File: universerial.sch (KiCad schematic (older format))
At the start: 11 parts

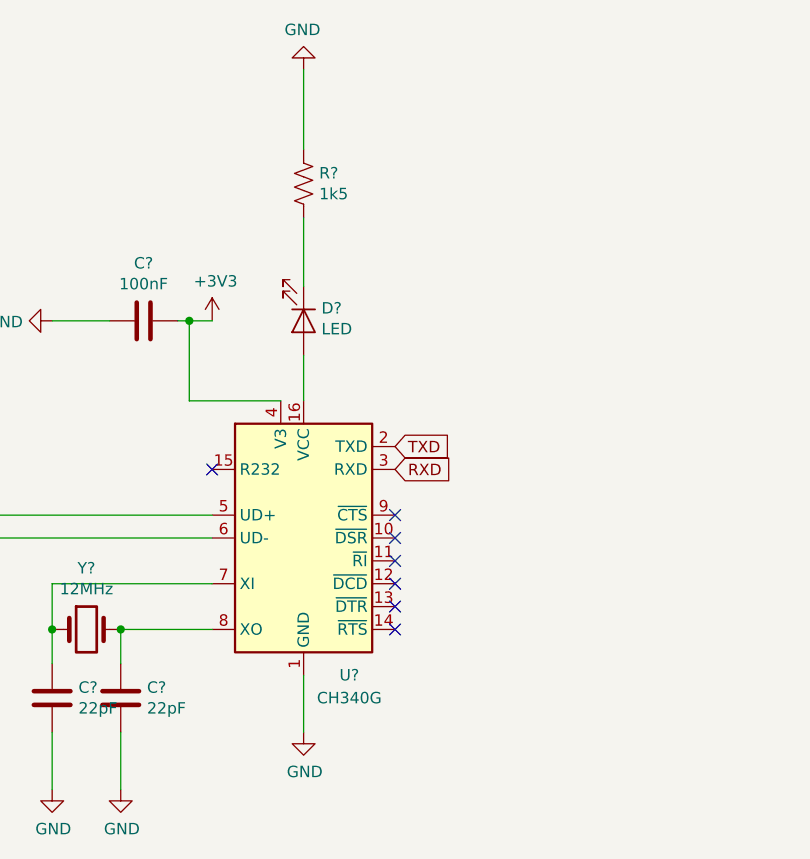
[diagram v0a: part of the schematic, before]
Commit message: Fix VCC placement.
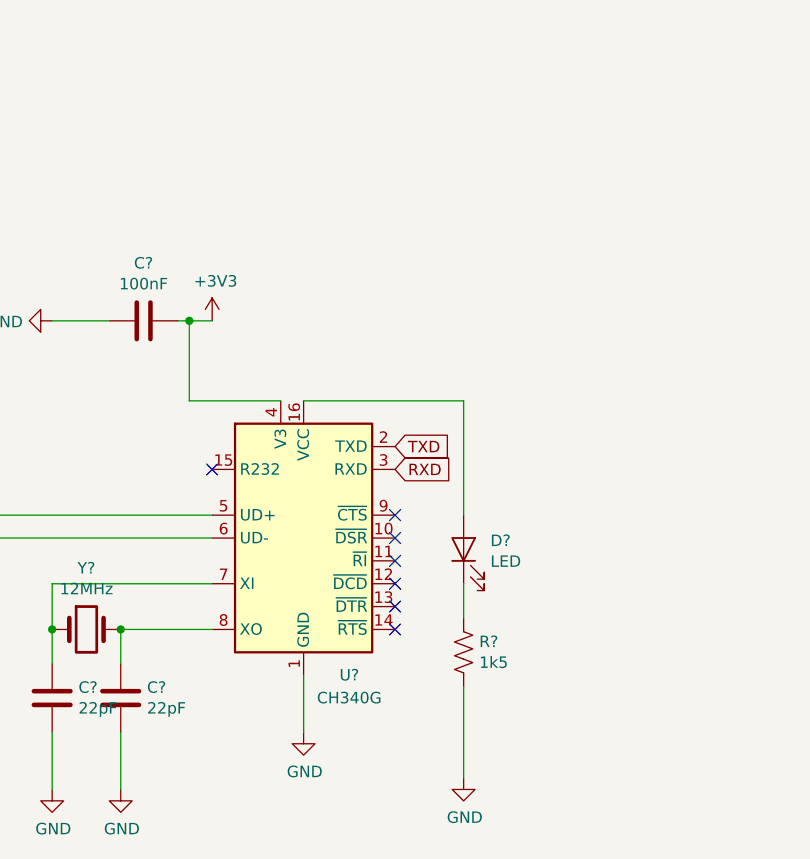
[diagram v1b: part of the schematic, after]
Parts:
- removed D?: LED, symbol Device:LED
- removed R?: 1k5, symbol Device:R_US
- added D?: LED, symbol Device:LED
- added R?: 1k5, symbol Device:R_US
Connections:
- net GND: now also R?.1
- net at U?.16 (VCC): now also D?.2 (A)
- new net: D?.1 (K), R?.2
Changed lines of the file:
@@
 	4950 2900 4900 2900
-$Comp
-L Device:LED D?
-U 1 1 610C1465
-P 5450 2900
-F 0 "D?" V 5395 2978 50  0000 L CNN
-F 1 "LED" V 5486 2978 50  0000 L CNN
-F 2 "" H 5450 2900 50  0001 C CNN
-F 3 "~" H 5450 2900 50  0001 C CNN
-	1    5450 2900
-	0    1    1    0
-$EndComp
-$Comp
-L Device:R_US R?
-U 1 1 610C1517
-P 5450 2300
-F 0 "R?" H 5518 2346 50  0000 L CNN
-F 1 "1k5" H 5518 2255 50  0000 L CNN
-F 2 "" V 5490 2290 50  0001 C CNN
-F 3 "~" H 5450 2300 50  0001 C CNN
-	1    5450 2300
-	1    0    0    -1
-$EndComp
-$Comp
-L power:GND #PWR?
-U 1 1 610C1658
-P 5450 1800
-F 0 "#PWR?" H 5450 1550 50  0001 C CNN
-F 1 "GND" H 5455 1627 50  0000 C CNN
-F 2 "" H 5450 1800 50  0001 C CNN
-F 3 "" H 5450 1800 50  0001 C CNN
-	1    5450 1800
-	-1   0    0    1
-$EndComp
-Wire Wire Line
-	5450 3250 5450 3050
-Wire Wire Line
-	5450 2750 5450 2450
-Wire Wire Line
-	5450 2150 5450 1800
 $Comp
 L Device:Crystal Y?
@@
 NoConn ~ 5850 3950
 NoConn ~ 5850 4050
+$Comp
+L Device:LED D?
+U 1 1 610C66BC
+P 6150 3900
+F 0 "D?" V 6188 3783 50  0000 R CNN
+F 1 "LED" V 6097 3783 50  0000 R CNN
+F 2 "" H 6150 3900 50  0001 C CNN
+F 3 "~" H 6150 3900 50  0001 C CNN
+	1    6150 3900
+	0    -1   -1   0
+$EndComp
+$Comp
+L Device:R_US R?
+U 1 1 610C671C
+P 6150 4350
+F 0 "R?" H 6082 4304 50  0000 R CNN
+F 1 "1k5" H 6082 4395 50  0000 R CNN
+F 2 "" V 6190 4340 50  0001 C CNN
+F 3 "~" H 6150 4350 50  0001 C CNN
+	1    6150 4350
+	-1   0    0    1
+$EndComp
+$Comp
+L power:GND #PWR?
+U 1 1 610C67B6
+P 6150 4900
+F 0 "#PWR?" H 6150 4650 50  0001 C CNN
+F 1 "GND" H 6155 4727 50  0000 C CNN
+F 2 "" H 6150 4900 50  0001 C CNN
+F 3 "" H 6150 4900 50  0001 C CNN
+	1    6150 4900
+	1    0    0    -1
+$EndComp
+Wire Wire Line
+	5450 3250 6150 3250
+Wire Wire Line
+	6150 3250 6150 3750
+Wire Wire Line
+	6150 4050 6150 4200
+Wire Wire Line
+	6150 4500 6150 4900
 $EndSCHEMATC

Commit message: Finish schematic.
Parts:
- added C?: 100nF, symbol Device:C
- added D? (x2): D, symbol Device:D
- added D? (x2): LED, symbol Device:LED
- added R? (x3): 1k5, symbol Device:R_US
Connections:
- net RXD is gone; now on an unnamed net: U?.3 (RXD)
- net +3V3: now also J?.3 (Pin_3)
- net +5V: now also J?.1 (Pin_1), D?.2 (A)
- net GND: now also J?.6 (Pin_6), C?.2
- net at D?.2 (A), U?.16 (VCC): now also J?.2 (Pin_2), C?.1, D?.1 (K), R?.1, R?.1
- net at J?.4 (Pin_4): now also R?.1
- net at J?.5 (Pin_5): now also D?.1 (K)
- net TXD: no longer names the net of U?.2 (TXD)
- net TXD: now also D?.1 (K), R?.2
- new net: D?.1 (K), D?.2 (A)
- new net: D?.2 (A), R?.2 (x2)
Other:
- moved on the sheet: C?, D?, J?, R?

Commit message: Annotate schematic.
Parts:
- gave numbers to parts that had none: 19
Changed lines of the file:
@@
 NoConn ~ 9500 3500
 $Comp
-L Connector_Generic:Conn_01x06 J?
+L Connector_Generic:Conn_01x06 J2
 U 1 1 610BFF68
 P 7800 3350
-F 0 "J?" H 7880 3342 50  0000 L CNN
+F 0 "J2" H 7880 3342 50  0000 L CNN
 F 1 "Conn_01x06" H 7880 3251 50  0000 L CNN
 F 2 "" H 7800 3350 50  0001 C CNN
@@
 $EndComp
 $Comp
-L Connector:USB_A J?
+L Connector:USB_A J1
 U 1 1 610C021E
 P 2800 3750
-F 0 "J?" H 2855 4217 50  0000 C CNN
+F 0 "J1" H 2855 4217 50  0000 C CNN
 F 1 "USB_A" H 2855 4126 50  0000 C CNN
 F 2 "" H 2950 3700 50  0001 C CNN
@@
 $EndComp
 $Comp
-L power:+5V #PWR?
+L power:+5V #PWR03
 U 1 1 610C0316
 P 3700 3150
-F 0 "#PWR?" H 3700 3000 50  0001 C CNN
+F 0 "#PWR03" H 3700 3000 50  0001 C CNN
 F 1 "+5V" H 3715 3323 50  0000 C CNN
 F 2 "" H 3700 3150 50  0001 C CNN
@@
 	3100 3550 3300 3550
 $Comp
-L power:GND #PWR?
+L power:GND #PWR01
 U 1 1 610C03FA
 P 2800 4350
-F 0 "#PWR?" H 2800 4100 50  0001 C CNN
+F 0 "#PWR01" H 2800 4100 50  0001 C CNN
 F 1 "GND" H 2805 4177 50  0000 C CNN
 F 2 "" H 2800 4350 50  0001 C CNN
@@
 	2800 4250 2800 4350
 $Comp
-L Device:C C?
+L Device:C C1
 U 1 1 610C04CB
 P 3300 4400
-F 0 "C?" H 3415 4446 50  0000 L CNN
+F 0 "C1" H 3415 4446 50  0000 L CNN
 F 1 "10uF" H 3415 4355 50  0000 L CNN
 F 2 "" H 3338 4250 50  0001 C CNN
@@
 	3300 3550 3300 4250
 $Comp
-L power:GND #PWR?
+L power:GND #PWR02
 U 1 1 610C055C
 P 3300 4800
-F 0 "#PWR?" H 3300 4550 50  0001 C CNN
+F 0 "#PWR02" H 3300 4550 50  0001 C CNN
 F 1 "GND" H 3305 4627 50  0000 C CNN
 F 2 "" H 3300 4800 50  0001 C CNN
@@
 	3300 4550 3300 4800
 $Comp
-L Device:C C?
+L Device:C C2
 U 1 1 610C09D3
 P 3700 4400
-F 0 "C?" H 3815 4446 50  0000 L CNN
+F 0 "C2" H 3815 4446 50  0000 L CNN
 F 1 "100nF" H 3815 4355 50  0000 L CNN
 F 2 "" H 3738 4250 50  0001 C CNN
@@
 $EndComp
 $Comp
-L power:GND #PWR?
+L power:GND #PWR04
 U 1 1 610C0A9A
 P 3700 4800
-F 0 "#PWR?" H 3700 4550 50  0001 C CNN
+F 0 "#PWR04" H 3700 4550 50  0001 C CNN
 F 1 "GND" H 3705 4627 50  0000 C CNN
 F 2 "" H 3700 4800 50  0001 C CNN
@@
 	3700 3550 3700 4250
 $Comp
-L power:+3V3 #PWR?
+L power:+3V3 #PWR08
 U 1 1 610C0EF4
 P 5050 2900
-F 0 "#PWR?" H 5050 2750 50  0001 C CNN
+F 0 "#PWR08" H 5050 2750 50  0001 C CNN
 F 1 "+3V3" H 5065 3073 50  0000 C CNN
 F 2 "" H 5050 2900 50  0001 C CNN
@@
 $EndComp
 $Comp
-L Device:C C?
+L Device:C C5
 U 1 1 610C0F5D
 P 4750 2900
-F 0 "C?" V 4498 2900 50  0000 C CNN
+F 0 "C5" V 4498 2900 50  0000 C CNN
 F 1 "100nF" V 4589 2900 50  0000 C CNN
 F 2 "" H 4788 2750 50  0001 C CNN
@@
 $EndComp
 $Comp
-L power:GND #PWR?
+L power:GND #PWR05
 U 1 1 610C0FF6
 P 4350 2900
-F 0 "#PWR?" H 4350 2650 50  0001 C CNN
+F 0 "#PWR05" H 4350 2650 50  0001 C CNN
 F 1 "GND" V 4355 2772 50  0000 R CNN
 F 2 "" H 4350 2900 50  0001 C CNN
@@
 	4950 2900 4900 2900
 $Comp
-L Device:Crystal Y?
+L Device:Crystal Y1
 U 1 1 610C1DB2
 P 4500 4250
-F 0 "Y?" H 4500 4518 50  0000 C CNN
+F 0 "Y1" H 4500 4518 50  0000 C CNN
 F 1 "12MHz" H 4500 4427 50  0000 C CNN
 F 2 "" H 4500 4250 50  0001 C CNN
@@
 $EndComp
 $Comp
-L power:GND #PWR?
+L power:GND #PWR09
 U 1 1 610C3384
 P 5450 4700
-F 0 "#PWR?" H 5450 4450 50  0001 C CNN
+F 0 "#PWR09" H 5450 4450 50  0001 C CNN
 F 1 "GND" H 5455 4527 50  0000 C CNN
 F 2 "" H 5450 4700 50  0001 C CNN
@@
 	5050 4250 4650 4250
 $Comp
-L Device:C C?
+L Device:C C3
 U 1 1 610C3F04
 P 4350 4550
-F 0 "C?" H 4465 4596 50  0000 L CNN
+F 0 "C3" H 4465 4596 50  0000 L CNN
 F 1 "22pF" H 4465 4505 50  0000 L CNN
 F 2 "" H 4388 4400 50  0001 C CNN
@@
 $EndComp
 $Comp
-L Device:C C?
+L Device:C C4
 U 1 1 610C3F3C
 P 4650 4550
-F 0 "C?" H 4765 4596 50  0000 L CNN
+F 0 "C4" H 4765 4596 50  0000 L CNN
 F 1 "22pF" H 4765 4505 50  0000 L CNN
 F 2 "" H 4688 4400 50  0001 C CNN
@@
 $EndComp
 $Comp
-L power:GND #PWR?
+L power:GND #PWR06
 U 1 1 610C3FDC
 P 4350 4950
-F 0 "#PWR?" H 4350 4700 50  0001 C CNN
+F 0 "#PWR06" H 4350 4700 50  0001 C CNN
 F 1 "GND" H 4355 4777 50  0000 C CNN
 F 2 "" H 4350 4950 50  0001 C CNN
@@
 $EndComp
 $Comp
-L power:GND #PWR?
+L power:GND #PWR07
 U 1 1 610C4004
 P 4650 4950
-F 0 "#PWR?" H 4650 4700 50  0001 C CNN
+F 0 "#PWR07" H 4650 4700 50  0001 C CNN
 F 1 "GND" H 4655 4777 50  0000 C CNN
 F 2 "" H 4650 4950 50  0001 C CNN
@@
 NoConn ~ 5850 4050
 $Comp
-L Device:LED D?
+L Device:LED D1
 U 1 1 610C66BC
 P 6000 3900
-F 0 "D?" V 6038 3783 50  0000 R CNN
+F 0 "D1" V 6038 3783 50  0000 R CNN
 F 1 "LED" V 5947 3783 50  0000 R CNN
 F 2 "" H 6000 3900 50  0001 C CNN
@@
 $EndComp
 $Comp
-L Device:R_US R?
+L Device:R_US R1
 U 1 1 610C671C
 P 6000 4350
-F 0 "R?" H 5932 4304 50  0000 R CNN
+F 0 "R1" H 5932 4304 50  0000 R CNN
 F 1 "1k5" H 5932 4395 50  0000 R CNN
 F 2 "" V 6040 4340 50  0001 C CNN
@@
 $EndComp
 $Comp
-L power:GND #PWR?
+L power:GND #PWR010
 U 1 1 610C67B6
 P 6000 4900
-F 0 "#PWR?" H 6000 4650 50  0001 C CNN
+F 0 "#PWR010" H 6000 4650 50  0001 C CNN
 F 1 "GND" H 6005 4727 50  0000 C CNN
 F 2 "" H 6000 4900 50  0001 C CNN
@@
 	6000 4500 6000 4900
 $Comp
-L power:+5V #PWR?
+L power:+5V #PWR014
 U 1 1 610C98EA
 P 7600 2850
-F 0 "#PWR?" H 7600 2700 50  0001 C CNN
+F 0 "#PWR014" H 7600 2700 50  0001 C CNN
 F 1 "+5V" H 7615 3023 50  0000 C CNN
 F 2 "" H 7600 2850 50  0001 C CNN
@@
 	7600 3150 7600 2850
 $Comp
-L power:GND #PWR?
+L power:GND #PWR015
 U 1 1 610C9D6A
 P 7600 3950
-F 0 "#PWR?" H 7600 3700 50  0001 C CNN
+F 0 "#PWR015" H 7600 3700 50  0001 C CNN
 F 1 "GND" H 7605 3777 50  0000 C CNN
 F 2 "" H 7600 3950 50  0001 C CNN
@@
 	7600 3650 7600 3950
 $Comp
-L power:+3V3 #PWR?
+L power:+3V3 #PWR013
 U 1 1 610CA266
 P 7450 3350
-F 0 "#PWR?" H 7450 3200 50  0001 C CNN
+F 0 "#PWR013" H 7450 3200 50  0001 C CNN
 F 1 "+3V3" H 7465 3523 50  0000 C CNN
 F 2 "" H 7450 3350 50  0001 C CNN
@@
 	7450 3350 7600 3350
 $Comp
-L Device:R_US R?
+L Device:R_US R4
 U 1 1 610CA74E
 P 7200 3450
-F 0 "R?" V 6995 3450 50  0000 C CNN
+F 0 "R4" V 6995 3450 50  0000 C CNN
 F 1 "1k5" V 7086 3450 50  0000 C CNN
 F 2 "" V 7240 3440 50  0001 C CNN
@@
 	5850 3450 6500 3450
 $Comp
-L Device:D D?
+L Device:D D5
 U 1 1 610CD045
 P 7050 2400
-F 0 "D?" H 7050 2184 50  0000 C CNN
+F 0 "D5" H 7050 2184 50  0000 C CNN
 F 1 "D" H 7050 2275 50  0000 C CNN
 F 2 "" H 7050 2400 50  0001 C CNN
@@
 $EndComp
 $Comp
-L Device:D D?
+L Device:D D3
 U 1 1 610CD0CD
 P 6600 2400
-F 0 "D?" H 6600 2184 50  0000 C CNN
+F 0 "D3" H 6600 2184 50  0000 C CNN
 F 1 "D" H 6600 2275 50  0000 C CNN
 F 2 "" H 6600 2400 50  0001 C CNN
@@
 $EndComp
 $Comp
-L power:+5V #PWR?
+L power:+5V #PWR012
 U 1 1 610CD241
 P 6300 2400
-F 0 "#PWR?" H 6300 2250 50  0001 C CNN
+F 0 "#PWR012" H 6300 2250 50  0001 C CNN
 F 1 "+5V" H 6315 2573 50  0000 C CNN
 F 2 "" H 6300 2400 50  0001 C CNN
@@
 	6450 2400 6300 2400
 $Comp
-L Device:C C?
+L Device:C C6
 U 1 1 610CF24E
 P 6200 2800
-F 0 "C?" H 6315 2846 50  0000 L CNN
+F 0 "C6" H 6315 2846 50  0000 L CNN
 F 1 "100nF" H 6315 2755 50  0000 L CNN
 F 2 "" H 6238 2650 50  0001 C CNN
@@
 $EndComp
 $Comp
-L Device:R_US R?
+L Device:R_US R2
 U 1 1 610D05C1
 P 6500 2800
-F 0 "R?" H 6568 2846 39  0000 L CNN
+F 0 "R2" H 6568 2846 39  0000 L CNN
 F 1 "1k5" H 6568 2763 50  0000 L CNN
 F 2 "" V 6540 2790 10  0001 C CNN
@@
 	6000 2650 6000 3750
 $Comp
-L power:GND #PWR?
+L power:GND #PWR011
 U 1 1 610D73AA
 P 6200 3050
-F 0 "#PWR?" H 6200 2800 50  0001 C CNN
+F 0 "#PWR011" H 6200 2800 50  0001 C CNN
 F 1 "GND" H 6205 2877 50  0000 C CNN
 F 2 "" H 6200 3050 50  0001 C CNN
@@
 	6200 2950 6200 3050
 $Comp
-L Device:LED D?
+L Device:LED D2
 U 1 1 610D7DE3
 P 6500 3150
-F 0 "D?" V 6538 3033 50  0000 R CNN
+F 0 "D2" V 6538 3033 50  0000 R CNN
 F 1 "LED" V 6447 3033 50  0000 R CNN
 F 2 "" H 6500 3150 50  0001 C CNN
@@
 	6500 3450 7050 3450
 $Comp
-L Device:R_US R?
+L Device:R_US R3
 U 1 1 610DB719
 P 6850 2800
-F 0 "R?" H 6918 2846 50  0000 L CNN
+F 0 "R3" H 6918 2846 50  0000 L CNN
 F 1 "1k5" H 6918 2755 50  0000 L CNN
 F 2 "" V 6890 2790 50  0001 C CNN
@@
 	6850 2650 7500 2650
 $Comp
-L Device:LED D?
+L Device:LED D4
 U 1 1 610DB7E0
 P 6850 3200
-F 0 "D?" V 6888 3083 50  0000 R CNN
+F 0 "D4" V 6888 3083 50  0000 R CNN
 F 1 "LED" V 6797 3083 50  0000 R CNN
 F 2 "" H 6850 3200 50  0001 C CNN
@@
 	3100 3750 5050 3750
 $Comp
-L Interface_USB:CH340G U?
+L Interface_USB:CH340G U1
 U 1 1 610BFB66
 P 5450 3850
-F 0 "U?" H 5650 3250 50  0000 C CNN
+F 0 "U1" H 5650 3250 50  0000 C CNN
 F 1 "CH340G" H 5650 3150 50  0000 C CNN
 F 2 "Package_SO:SOIC-16_3.9x9.9mm_P1.27mm" H 5500 3300 50  0001 L CNN

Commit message: Assign footprints.
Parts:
- C1, C2, C3, C4, C5, C6: footprint (none) -> Capacitor_SMD:C_0201_0603Metric
- D1, D2, D4: footprint (none) -> LED_SMD:LED-L1T2_LUMILEDS
- D3, D5: footprint (none) -> Diode_SMD:D_0201_0603Metric
- J1: footprint (none) -> Connector_USB:USB_A_CNCTech_1001-011-01101_Horizontal
- J2: footprint (none) -> Connector_Harwin:Harwin_M20-89006xx_1x06_P2.54mm_Horizontal
- R1, R2, R3, R4: footprint (none) -> Resistor_SMD:R_0201_0603Metric
- Y1: footprint (none) -> Crystal:Crystal_AT310_D3.0mm_L10.0mm_Horizontal
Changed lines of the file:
@@
 F 0 "J2" H 7880 3342 50  0000 L CNN
 F 1 "Conn_01x06" H 7880 3251 50  0000 L CNN
-F 2 "" H 7800 3350 50  0001 C CNN
+F 2 "Connector_Harwin:Harwin_M20-89006xx_1x06_P2.54mm_Horizontal" H 7800 3350 50  0001 C CNN
 F 3 "~" H 7800 3350 50  0001 C CNN
 	1    7800 3350
@@
 F 0 "J1" H 2855 4217 50  0000 C CNN
 F 1 "USB_A" H 2855 4126 50  0000 C CNN
-F 2 "" H 2950 3700 50  0001 C CNN
+F 2 "Connector_USB:USB_A_CNCTech_1001-011-01101_Horizontal" H 2950 3700 50  0001 C CNN
 F 3 " ~" H 2950 3700 50  0001 C CNN
 	1    2800 3750
@@
 F 0 "C1" H 3415 4446 50  0000 L CNN
 F 1 "10uF" H 3415 4355 50  0000 L CNN
-F 2 "" H 3338 4250 50  0001 C CNN
+F 2 "Capacitor_SMD:C_0201_0603Metric" H 3338 4250 50  0001 C CNN
 F 3 "~" H 3300 4400 50  0001 C CNN
 	1    3300 4400
@@
 F 0 "C2" H 3815 4446 50  0000 L CNN
 F 1 "100nF" H 3815 4355 50  0000 L CNN
-F 2 "" H 3738 4250 50  0001 C CNN
+F 2 "Capacitor_SMD:C_0201_0603Metric" H 3738 4250 50  0001 C CNN
 F 3 "~" H 3700 4400 50  0001 C CNN
 	1    3700 4400
@@
 F 0 "C5" V 4498 2900 50  0000 C CNN
 F 1 "100nF" V 4589 2900 50  0000 C CNN
-F 2 "" H 4788 2750 50  0001 C CNN
+F 2 "Capacitor_SMD:C_0201_0603Metric" H 4788 2750 50  0001 C CNN
 F 3 "~" H 4750 2900 50  0001 C CNN
 	1    4750 2900
@@
 F 0 "Y1" H 4500 4518 50  0000 C CNN
 F 1 "12MHz" H 4500 4427 50  0000 C CNN
-F 2 "" H 4500 4250 50  0001 C CNN
+F 2 "Crystal:Crystal_AT310_D3.0mm_L10.0mm_Horizontal" H 4500 4250 50  0001 C CNN
 F 3 "~" H 4500 4250 50  0001 C CNN
 	1    4500 4250
@@
 F 0 "C3" H 4465 4596 50  0000 L CNN
 F 1 "22pF" H 4465 4505 50  0000 L CNN
-F 2 "" H 4388 4400 50  0001 C CNN
+F 2 "Capacitor_SMD:C_0201_0603Metric" H 4388 4400 50  0001 C CNN
 F 3 "~" H 4350 4550 50  0001 C CNN
 	1    4350 4550
@@
 F 0 "C4" H 4765 4596 50  0000 L CNN
 F 1 "22pF" H 4765 4505 50  0000 L CNN
-F 2 "" H 4688 4400 50  0001 C CNN
+F 2 "Capacitor_SMD:C_0201_0603Metric" H 4688 4400 50  0001 C CNN
 F 3 "~" H 4650 4550 50  0001 C CNN
 	1    4650 4550
@@
 F 0 "D1" V 6038 3783 50  0000 R CNN
 F 1 "LED" V 5947 3783 50  0000 R CNN
-F 2 "" H 6000 3900 50  0001 C CNN
+F 2 "LED_SMD:LED-L1T2_LUMILEDS" H 6000 3900 50  0001 C CNN
 F 3 "~" H 6000 3900 50  0001 C CNN
 	1    6000 3900
@@
 F 0 "R1" H 5932 4304 50  0000 R CNN
 F 1 "1k5" H 5932 4395 50  0000 R CNN
-F 2 "" V 6040 4340 50  0001 C CNN
+F 2 "Resistor_SMD:R_0201_0603Metric" V 6040 4340 50  0001 C CNN
 F 3 "~" H 6000 4350 50  0001 C CNN
 	1    6000 4350
@@
 F 0 "R4" V 6995 3450 50  0000 C CNN
 F 1 "1k5" V 7086 3450 50  0000 C CNN
-F 2 "" V 7240 3440 50  0001 C CNN
+F 2 "Resistor_SMD:R_0201_0603Metric" V 7240 3440 50  0001 C CNN
 F 3 "~" H 7200 3450 50  0001 C CNN
 	1    7200 3450
@@
 F 0 "D5" H 7050 2184 50  0000 C CNN
 F 1 "D" H 7050 2275 50  0000 C CNN
-F 2 "" H 7050 2400 50  0001 C CNN
+F 2 "Diode_SMD:D_0201_0603Metric" H 7050 2400 50  0001 C CNN
 F 3 "~" H 7050 2400 50  0001 C CNN
 	1    7050 2400
@@
 F 0 "D3" H 6600 2184 50  0000 C CNN
 F 1 "D" H 6600 2275 50  0000 C CNN
-F 2 "" H 6600 2400 50  0001 C CNN
+F 2 "Diode_SMD:D_0201_0603Metric" H 6600 2400 50  0001 C CNN
 F 3 "~" H 6600 2400 50  0001 C CNN
 	1    6600 2400
@@
 F 0 "C6" H 6315 2846 50  0000 L CNN
 F 1 "100nF" H 6315 2755 50  0000 L CNN
-F 2 "" H 6238 2650 50  0001 C CNN
+F 2 "Capacitor_SMD:C_0201_0603Metric" H 6238 2650 50  0001 C CNN
 F 3 "~" H 6200 2800 50  0001 C CNN
 	1    6200 2800
@@
 F 0 "R2" H 6568 2846 39  0000 L CNN
 F 1 "1k5" H 6568 2763 50  0000 L CNN
-F 2 "" V 6540 2790 10  0001 C CNN
+F 2 "Resistor_SMD:R_0201_0603Metric" V 6540 2790 10  0001 C CNN
 F 3 "~" H 6500 2800 50  0001 C CNN
 	1    6500 2800
@@
 F 0 "D2" V 6538 3033 50  0000 R CNN
 F 1 "LED" V 6447 3033 50  0000 R CNN
-F 2 "" H 6500 3150 50  0001 C CNN
+F 2 "LED_SMD:LED-L1T2_LUMILEDS" H 6500 3150 50  0001 C CNN
 F 3 "~" H 6500 3150 50  0001 C CNN
 	1    6500 3150
@@
 F 0 "R3" H 6918 2846 50  0000 L CNN
 F 1 "1k5" H 6918 2755 50  0000 L CNN
-F 2 "" V 6890 2790 50  0001 C CNN
+F 2 "Resistor_SMD:R_0201_0603Metric" V 6890 2790 50  0001 C CNN
 F 3 "~" H 6850 2800 50  0001 C CNN
 	1    6850 2800
@@
 F 0 "D4" V 6888 3083 50  0000 R CNN
 F 1 "LED" V 6797 3083 50  0000 R CNN
-F 2 "" H 6850 3200 50  0001 C CNN
+F 2 "LED_SMD:LED-L1T2_LUMILEDS" H 6850 3200 50  0001 C CNN
 F 3 "~" H 6850 3200 50  0001 C CNN
 	1    6850 3200
